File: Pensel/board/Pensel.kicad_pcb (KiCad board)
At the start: 2 copper layers, 60 x 13 mm, 189 parts, among them J1 TEST_1P, J2 Fiducial, J3 JTAG, J4 I2C, J5 Fiducial, J6 Fiducial, J7 Fiducial, J8 UART, P1 USB_PROC, SW1 RST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

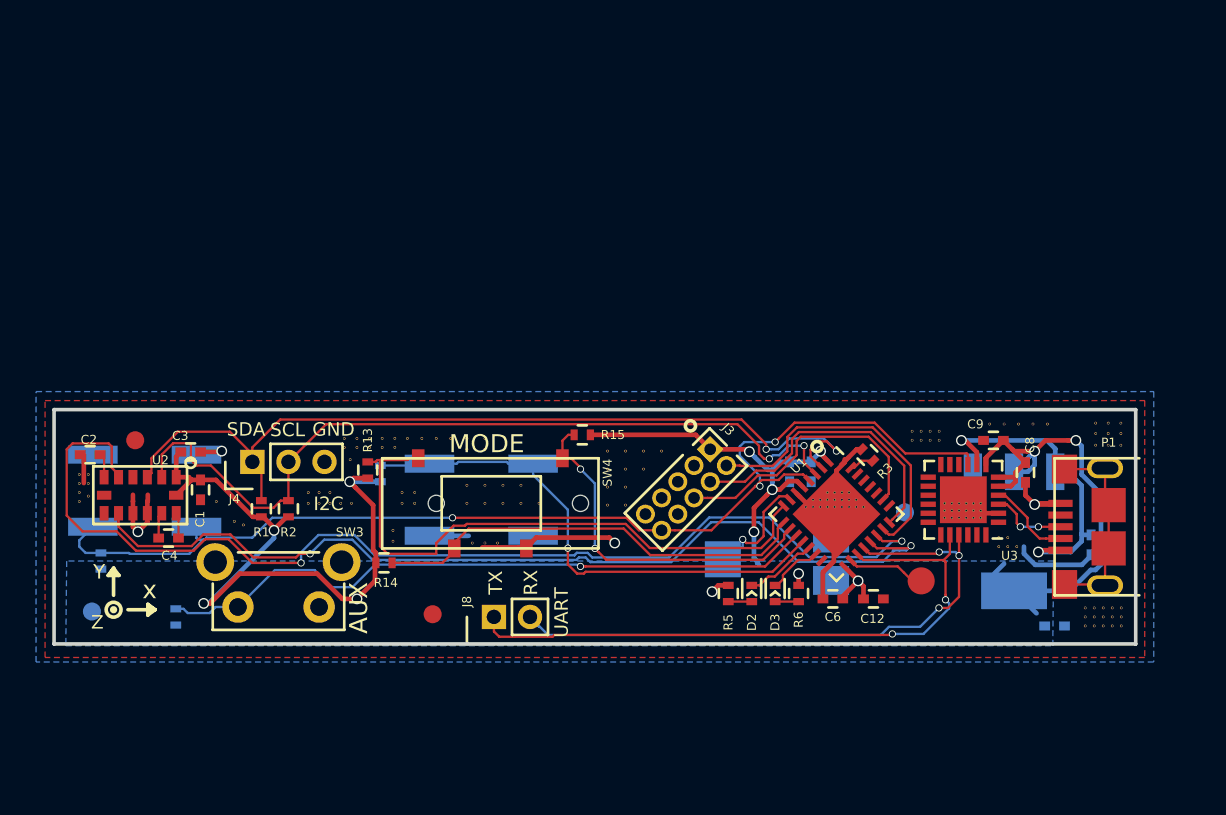
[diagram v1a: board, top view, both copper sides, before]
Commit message: Many changes supporting board revision 2.0
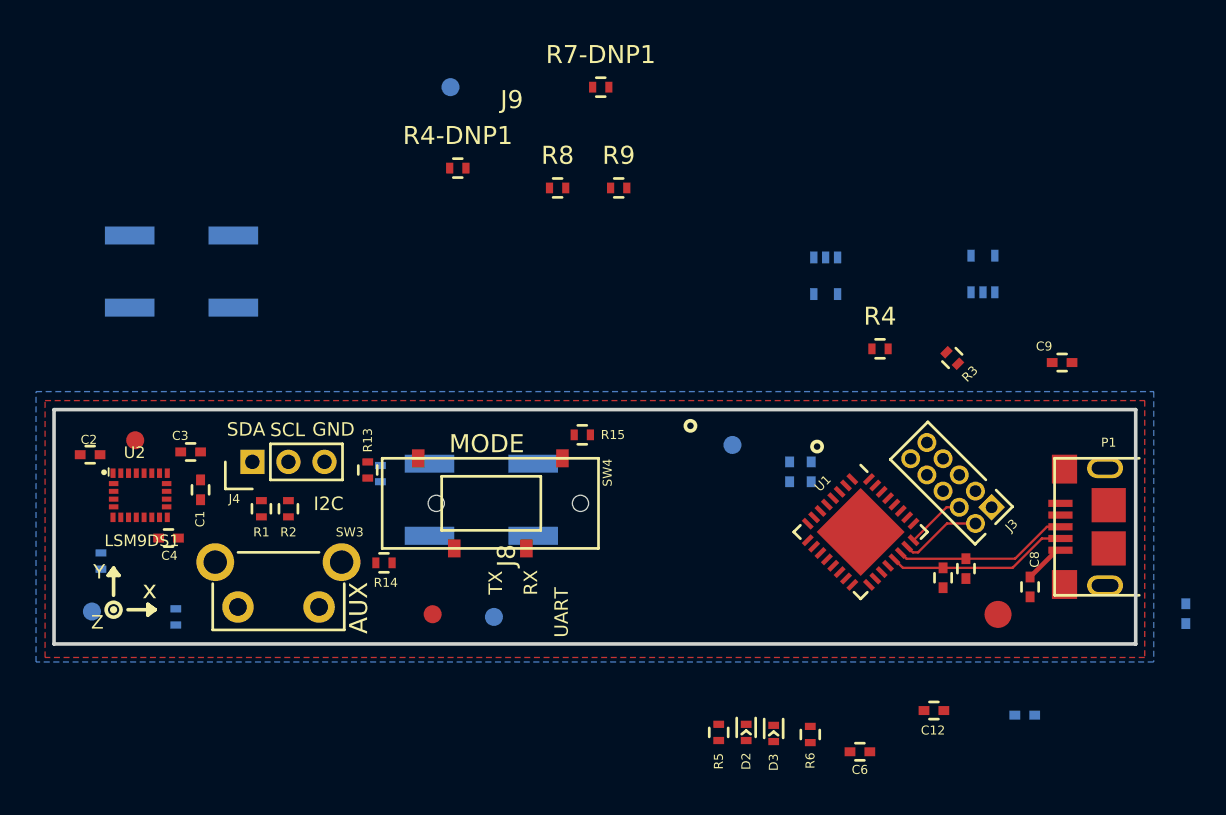
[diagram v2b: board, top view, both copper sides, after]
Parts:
- removed ? (x146): via-1.0mm, TylerCustom:via-1.0mm
- removed RV10K1: THUMBWHEEL, TylerCustom:ST-4
- added C_NOSTUFF1: 0.1 uF, Capacitors_SMD:C_0402, F.Cu at (100.6, 147.3)
- added C_NOSTUFF2: 0.1 uF, Capacitors_SMD:C_0402, F.Cu at (99.3, 147.8)
- added J9: UART_RX, Fiducials:Fiducial_1mm_Dia_2.54mm_Outer_CopperBottom, F.Cu at (72.0, 120.6)
- added R4: 4K7, Resistors_SMD:R_0402, F.Cu at (95.8, 135.1)
- added R4-DNP1: 4K7, Resistors_SMD:R_0402, F.Cu at (72.4, 125.1)
- added R7-DNP1: 4K7, Resistors_SMD:R_0402, F.Cu at (80.3, 120.6)
- added R8: 4K7, Resistors_SMD:R_0402, F.Cu at (77.9, 126.2)
- added R9: 4K7, Resistors_SMD:R_0402, F.Cu at (81.3, 126.2)
- C1: value 4.7 uF -> 10 nF
- C2: value 4.7 uF -> 0.1 uF
- C3: value 0.1 uF -> 10 nF
- C4: value 0.22 uF -> 0.1 uF
- C8: value 4.7 uF -> 1 uF
- C9: value 0.1 uF -> 1 uF
- J8: value UART -> UART_TX; footprint Pin_Headers:Pin_Header_Straight_1x02_Pitch2.00mm -> Fiducials:Fiducial_1mm_Dia_2.54mm_Outer_CopperBottom
- U2: value LSM303DLHC -> LSM9DS1; footprint TylerCustom:LGA_14L_3mm_5mm -> LSM9DS1:PQFN24P43_350X300X102L35X23N
- U3: value CP2102N-A01-GQFN24 -> NCP114; footprint Housings_DFN_QFN:QFN-24-1EP_4x4mm_Pitch0.5mm -> TO_SOT_Packages_SMD:SC-70-5; moved to B.Cu
- U4: value AP111733 -> NCP508; footprint TO_SOT_Packages_SMD:SOT-223 -> TO_SOT_Packages_SMD:SC-70-5
- moved U4 17.6 mm to (92.8, 131.1)
- moved J3 15.9 mm to (102.0, 143.9), turned to 225 degrees
- moved U3 12.6 mm to (101.5, 131.0)
- moved SW1 12.3 mm to (57.1, 130.8)
- moved J2 10.3 mm to (87.6, 140.5)
- moved C6 8.61 mm to (94.7, 157.5)
- moved R6 7.85 mm to (91.9, 156.5)
- moved D3 7.76 mm to (89.9, 156.5)
- moved R5 7.72 mm to (86.9, 156.4)
- moved D2 7.71 mm to (88.4, 156.4)
- moved R3 7.15 mm to (99.8, 135.6)
- moved C12 7.04 mm to (98.8, 155.2)
- moved C11 6.49 mm to (112.8, 149.8)
- moved C8 6.36 mm to (104.1, 148.3)
- moved C9 5.76 mm to (105.9, 135.9)
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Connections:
- net Net-(J1-Pad1) renamed /test_pin
- net Net-(R3-Pad1) renamed /boot
- C1 pad 1: +3V3 -> +3.3VA
- C2 pad 1: Net-(C2-Pad1) -> +3.3VA
- C3 pad 1: +3V3 -> Net-(C3-Pad1)
- C4 pad 2: Net-(C4-Pad2) -> GND
- C8 pad 1: +3V3 -> +5V
- C9 pad 1: +3V3 -> +3.3VA
- J3 pad 7: Net-(J3-Pad7) -> (no net)
- J3 pad 8: Net-(J3-Pad8) -> (no net)
- P1 pad 2: Net-(P1-Pad2) -> /USB_n
- P1 pad 3: Net-(P1-Pad3) -> /USB_p
- P1 pad 4: Net-(P1-Pad4) -> (no net)
- U1 pad 15: Net-(U1-Pad15) -> (no net)
- U1 pad 19: DBG_UART_TX -> (no net)
- U1 pad 20: DBG_UART_RX -> (no net)
- U1 pad 21: SEN_DRDY -> /USB_n
- U1 pad 22: SEN_INT1 -> /USB_p
- U1 pad 25: Net-(U1-Pad25) -> (no net)
- U1 pad 27: Net-(U1-Pad27) -> (no net)
- U1 pad 28: Net-(U1-Pad28) -> (no net)
- U1 pad 29: Net-(U1-Pad29) -> BREV-0
- U1 pad 30: Net-(U1-Pad30) -> BREV-1
- U1 pad 5: +3V3 -> +3.3VA
- U1 pad 7: THUMBWHEEL -> (no net)
- U2 pad 10: GND -> (no net)
- U2 pad 11: GND -> (no net)
- U2 pad 12: Net-(C4-Pad2) -> (no net)
- U2 pad 13: Net-(C4-Pad1) -> +3V3
- U2 pad 14: +3V3 -> GND
- U2 pad 3: SDA -> +3V3
- U2 pad 4: Net-(U2-Pad4) -> SDA
- U2 pad 5: SEN_INT1 -> +3V3
- U2 pad 6: Net-(C2-Pad1) -> +3V3
- U2 pad 7: GND -> +3V3
- U2 pad 8: Net-(U2-Pad8) -> +3V3
- U2 pad 9: SEN_DRDY -> (no net)
- U3 pad 1: Net-(U3-Pad1) -> +5V
- U3 pad 3: Net-(P1-Pad3) -> +5V
- U3 pad 4: Net-(P1-Pad2) -> (no net)
- U4 pad 1: GND -> +5V
- U4 pad 2: +3V3 -> GND
- U4 pad 3: +5V -> +3V3
- U4 pad 4: +3V3 -> (no net)
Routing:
- net +3V3: track 94.1 -> 0.00 mm, vias 13 -> 0
- net RESET_n: track 63.1 -> 0.00 mm, vias 3 -> 0
- net SEN_INT1: track 61.8 -> 0.00 mm, vias 2 -> 0
- net SEN_DRDY: track 52.1 -> 0.00 mm, vias 2 -> 0
- net SDA: track 49.1 -> 0.00 mm, vias 2 -> 0
- net SCL: track 45.5 -> 0.00 mm, vias 2 -> 0
- net GND: track 38.0 -> 0.00 mm, vias 4 -> 0
- net BTN_AUX: track 37.2 -> 0.00 mm, vias 1 -> 0
- net DBG_UART_TX: track 36.2 -> 0.00 mm, vias 2 -> 0
- net DBG_UART_RX: track 34.8 -> 0.00 mm, vias 3 -> 0
- net MODE_0: track 33.8 -> 0.00 mm
- net BTN_MAIN: track 29.0 -> 0.00 mm, vias 1 -> 0
- net MODE_1: track 24.5 -> 0.00 mm
- net MODE_2: track 19.7 -> 0.00 mm, vias 2 -> 0
- net SWD-SWO: track 15.6 -> 0.00 mm
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- removed copper zone on B.Cu, net +3V3

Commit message: first time fully routed and placed v2
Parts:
- removed J8: UART_TX, Fiducials:Fiducial_1mm_Dia_2.54mm_Outer_CopperBottom
- removed J9: UART_RX, Fiducials:Fiducial_1mm_Dia_2.54mm_Outer_CopperBottom
- removed R4-DNP1, R7-DNP1: 4K7, Resistors_SMD:R_0402
- added ?: via-1.0mm, TylerCustom:via-1.0mm, F.Cu at (94.5, 145.5)
- added ?: via-1.0mm, TylerCustom:via-1.0mm, F.Cu at (94.5, 144.0)
- added ?: via-1.0mm, TylerCustom:via-1.0mm, F.Cu at (95.2, 144.0)
- added ?: via-1.0mm, TylerCustom:via-1.0mm, F.Cu at (96.8, 144.0)
- added ?: via-1.0mm, TylerCustom:via-1.0mm, F.Cu at (96.0, 144.0)
- added ?: via-1.0mm, TylerCustom:via-1.0mm, F.Cu at (96.0, 143.2)
- added ?: via-1.0mm, TylerCustom:via-1.0mm, F.Cu at (95.2, 143.2)
- added ?: via-1.0mm, TylerCustom:via-1.0mm, F.Cu at (94.5, 143.2)
- added ?: via-1.0mm, TylerCustom:via-1.0mm, F.Cu at (95.2, 142.5)
- added ?: via-1.0mm, TylerCustom:via-1.0mm, F.Cu at (94.5, 142.5)
- added ?: via-1.0mm, TylerCustom:via-1.0mm, F.Cu at (95.2, 145.5)
- added ?: via-1.0mm, TylerCustom:via-1.0mm, F.Cu at (96.0, 144.8)
- added ?: via-1.0mm, TylerCustom:via-1.0mm, F.Cu at (95.2, 144.8)
- added ?: via-1.0mm, TylerCustom:via-1.0mm, F.Cu at (94.5, 144.8)
- added ?: via-1.0mm, TylerCustom:via-1.0mm, F.Cu at (93.8, 144.8)
- added ?: via-1.0mm, TylerCustom:via-1.0mm, F.Cu at (93.0, 144.0)
- added ?: via-1.0mm, TylerCustom:via-1.0mm, F.Cu at (93.8, 143.2)
- added ?: via-1.0mm, TylerCustom:via-1.0mm, F.Cu at (93.8, 144.0)
- added C13: 0.1 uF, Capacitors_SMD:C_0402, F.Cu at (91.5, 141.2)
- added C14: 1 uF, Capacitors_SMD:C_0402, F.Cu at (89.8, 142.8)
- added JP1: Jumper, Resistors_SMD:R_0402, F.Cu at (108.0, 139.9)
- C1: value 10 nF -> 10 uF; footprint Capacitors_SMD:C_0402 -> Capacitors_SMD:c_elec_3x5.3
- C10, C11, C5, R10, R11, R12, U3, U4: moved to F.Cu
- C7: value 1 uF -> 0.1 uF; moved to F.Cu
- J4: value I2C -> COMS; footprint Pin_Headers:Pin_Header_Straight_1x03_Pitch2.00mm -> Pin_Headers:Pin_Header_Straight_1x06_Pitch2.00mm
- SW1: value RST -> TACT_4.2MM; footprint Buttons_Switches_SMD:SW_SPST_B3SL-1002P -> MF_Switches:MF_Switches-TACT4.2MM; moved to F.Cu
- SW3: footprint Buttons_Switches_ThroughHole:SW_Tactile_SPST_Angled -> Buttons_Switches_SMD:SW_SPST_B3SL-1002P
- moved R10 47.2 mm to (99.6, 143.1), turned to 180 degrees
- moved C12 46.3 mm to (53.1, 147.6), turned to 270 degrees
- moved R3 26.3 mm to (74.4, 142.5), turned to 270 degrees
- moved J4 25.5 mm to (85.1, 149.6), turned to 270 degrees
- moved R8 22.8 mm to (96.2, 139.8), turned to 45 degrees
- moved R9 21.5 mm to (97.2, 140.8), turned to 45 degrees
- moved U4 21.1 mm to (103.5, 149.3), turned to 180 degrees
- moved R1 19.0 mm to (80.3, 147.1), turned to 270 degrees
- moved U3 18.2 mm to (98.3, 148.8)
- moved SW2 17.8 mm to (56.0, 145.1)
- moved J2 17.5 mm to (102.7, 149.4)
- moved C6 16.0 mm to (90.7, 142.0), turned to 135 degrees
- moved SW1 15.7 mm to (69.3, 140.7), turned to 0 degrees
- moved R2 15.3 mm to (78.0, 147.1), turned to 270 degrees
- moved J5 15.2 mm to (64.0, 140.3)
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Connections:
- net /USB_n renamed /USB-
- net /USB_p renamed /USB+
- C6 pad 1: +3V3 -> +3.3VA
- J4 pad 1: SDA -> +3V3
- J4 pad 2: SCL -> UART_TX
- J4 pad 3: GND -> UART_RX
- R3 pad 1: /boot -> Net-(R3-Pad1)
- R4 pad 1: +3V3 -> Net-(R4-Pad1)
- R4 pad 2: GND -> +3V3
- SW1 pad 1: GND -> +3V3
- SW1 pad 2: RESET_n -> (no net)
- U1 pad 15: (no net) -> M_DRDY
- U1 pad 19: (no net) -> UART_TX
- U1 pad 20: (no net) -> UART_RX
- U1 pad 25: (no net) -> AG_INT2
- U1 pad 31: /boot -> Net-(R3-Pad1)
- U1 pad 7: (no net) -> AG_INT1
- U2 pad 11: (no net) -> AG_INT1
- U2 pad 12: (no net) -> AG_INT2
- U2 pad 9: (no net) -> M_DRDY
- U4 pad 3: +3V3 -> Net-(R4-Pad1)
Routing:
- net +3V3: track 0.00 -> 89.7 mm, vias 0 -> 8
- net GND: track 0.00 -> 88.2 mm, vias 0 -> 15
- net SDA: track 0.00 -> 64.7 mm, vias 0 -> 2
- net SCL: track 0.00 -> 63.0 mm, vias 0 -> 4
- net AG_INT2: track 0.00 -> 48.2 mm, vias 0 -> 2
- net BTN_MAIN: track 0.00 -> 45.4 mm, vias 0 -> 2
- net AG_INT1: track 0.00 -> 41.9 mm, vias 0 -> 4
- net M_DRDY: track 0.00 -> 41.4 mm, vias 0 -> 2
- net Net-(R3-Pad1): track 0.00 -> 35.7 mm
- net BTN_AUX: track 0.00 -> 31.6 mm, vias 0 -> 2
- net +3.3VA: track 0.00 -> 24.7 mm, vias 0 -> 4
- net MODE_0: track 0.00 -> 23.0 mm, vias 0 -> 2
- net UART_RX: track 0.00 -> 21.4 mm, vias 0 -> 1
- net UART_TX: track 0.00 -> 18.3 mm, vias 0 -> 1
- net MODE_1: track 0.00 -> 14.3 mm, vias 0 -> 2
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- added copper zone on In2.Cu, net +3.3VA
- added copper zone on In2.Cu, net +3V3
- added copper zone on In1.Cu, net GND
- removed copper zone on B.Cu, net GND
- removed copper zone on F.Cu, net GND
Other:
- copper layers 2 -> 4
- board text added: "2.0 3/18 Tyler Holmes"
- board text added: "DFU"
- board text removed: "1.0 3/17 Tyler Holmes"
- board text removed: "3V3"
- board text removed: "5V0"
- board text removed: "I2C"
- board text removed: "RST"
- board text removed: "SENSITIVITY"
- board text removed: "UART"

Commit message: finalized footprints and layout for v2 hopefully
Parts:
- C1: footprint Capacitors_SMD:c_elec_3x5.3 -> Capacitors_SMD:C_0603
- moved C1 2.12 mm to (56.9, 142.8), turned to 90 degrees
- moved SW2 0.56 mm to (55.5, 144.9)
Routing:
- net +3.3VA: track 24.7 -> 17.2 mm, vias 4 -> 3
- net GND: track 88.2 -> 87.1 mm
- net SDA: track 64.7 -> 63.6 mm
- net SCL: track 63.0 -> 62.0 mm

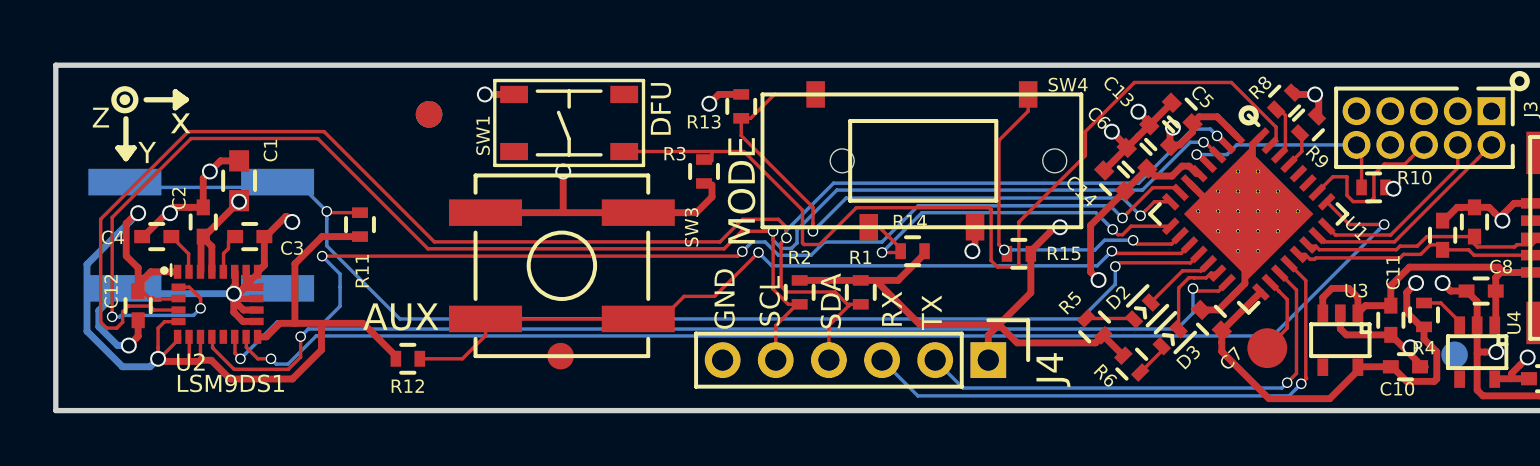
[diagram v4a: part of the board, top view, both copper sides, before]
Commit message: reorganize pins, add oscillator to support USB
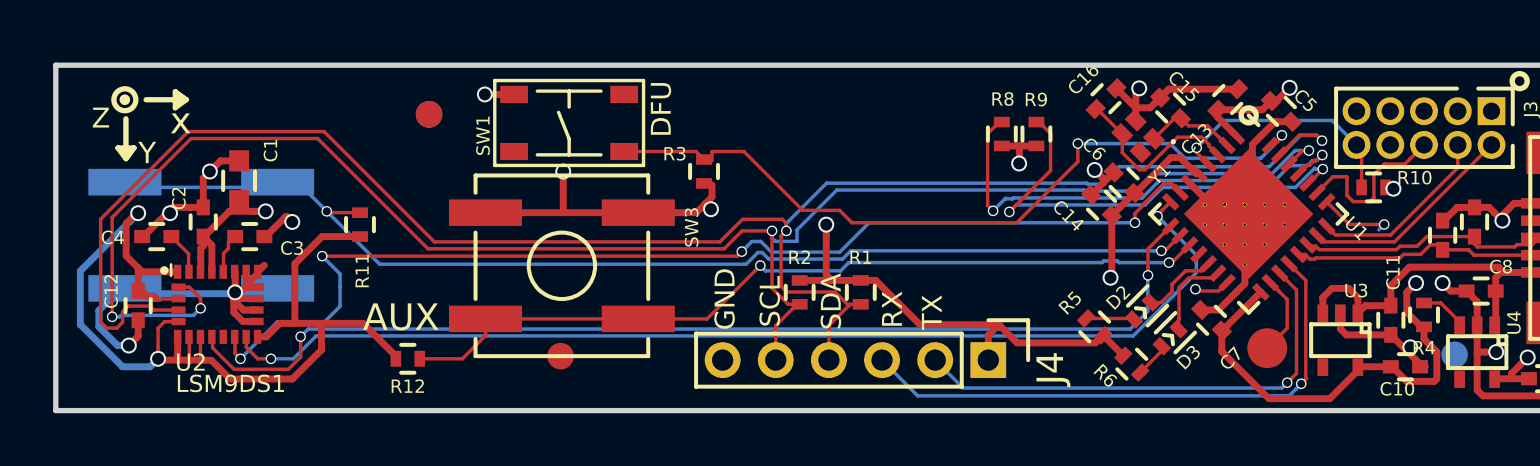
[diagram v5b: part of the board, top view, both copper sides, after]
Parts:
- removed the ? at (94.5, 145.5)
- removed the ? at (94.5, 144.0)
- removed the ? at (95.2, 144.0)
- removed the ? at (96.8, 144.0)
- removed the ? at (96.0, 144.0)
- removed the ? at (96.0, 143.2)
- removed the ? at (95.2, 143.2)
- removed the ? at (94.5, 143.2)
- removed the ? at (95.2, 142.5)
- removed the ? at (94.5, 142.5)
- removed the ? at (95.2, 145.5)
- removed the ? at (96.0, 144.8)
- removed the ? at (95.2, 144.8)
- removed the ? at (94.5, 144.8)
- removed the ? at (93.8, 144.8)
- removed the ? at (93.0, 144.0)
- removed the ? at (93.8, 143.2)
- removed the ? at (93.8, 144.0)
- removed R13, R14, R15: 4K7, Resistors_SMD:R_0402
- removed SW4: MODE_SEL, TylerCustom:CL-SB-13B-01
- added ?: via-1.0mm, TylerCustom:via-1.0mm, F.Cu at (94.0, 145.2)
- added ?: via-1.0mm, TylerCustom:via-1.0mm, F.Cu at (96.2, 143.8)
- added ?: via-1.0mm, TylerCustom:via-1.0mm, F.Cu at (96.2, 144.5)
- added ?: via-1.0mm, TylerCustom:via-1.0mm, F.Cu at (95.5, 144.5)
- added ?: via-1.0mm, TylerCustom:via-1.0mm, F.Cu at (95.5, 145.2)
- added ?: via-1.0mm, TylerCustom:via-1.0mm, F.Cu at (94.8, 145.2)
- added ?: via-1.0mm, TylerCustom:via-1.0mm, F.Cu at (94.8, 146.0)
- added ?: via-1.0mm, TylerCustom:via-1.0mm, F.Cu at (94.8, 144.5)
- added ?: via-1.0mm, TylerCustom:via-1.0mm, F.Cu at (94.0, 144.5)
- added ?: via-1.0mm, TylerCustom:via-1.0mm, F.Cu at (93.2, 144.5)
- added ?: via-1.0mm, TylerCustom:via-1.0mm, F.Cu at (93.2, 143.8)
- added ? (x2): via-1.0mm, TylerCustom:via-1.0mm, F.Cu at (94.0, 143.8)
- added ?: via-1.0mm, TylerCustom:via-1.0mm, F.Cu at (94.8, 143.8)
- added ?: via-1.0mm, TylerCustom:via-1.0mm, F.Cu at (95.5, 143.8)
- added C15: 8 pF, Capacitors_SMD:C_0402, F.Cu at (92.0, 140.1)
- added C16: 8 pF, Capacitors_SMD:C_0402, F.Cu at (89.5, 139.8)
- added Y1: 24 MHz, 416F32022CKR:OSCSC49P160X120X45-4N, F.Cu at (90.7, 141.2)
- moved R8 10.7 mm to (85.6, 141.1), turned to 270 degrees
- moved R9 10.2 mm to (86.9, 141.1), turned to 270 degrees
- moved C5 3.73 mm to (96.1, 140.2), turned to 315 degrees
- moved C13 2.90 mm to (94.1, 139.8), turned to 45 degrees
- moved C14 1.04 mm to (89.4, 143.8)
- moved C6 1.04 mm to (90.2, 142.9)
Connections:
- J3 pad 7: (no net) -> Net-(J3-Pad7)
- J3 pad 8: (no net) -> Net-(J3-Pad8)
- P1 pad 4: (no net) -> Net-(P1-Pad4)
- SW1 pad 2: (no net) -> Net-(SW1-Pad2)
- SW1 pad 3: (no net) -> Net-(SW1-Pad3)
- U1 pad 10: MODE_2 -> BTN_MAIN
- U1 pad 12: BTN_MAIN -> Net-(U1-Pad12)
- U1 pad 15: M_DRDY -> Net-(U1-Pad15)
- U1 pad 2: SDA -> Net-(C15-Pad1)
- U1 pad 25: AG_INT2 -> Net-(U1-Pad25)
- U1 pad 27: (no net) -> BREV-0
- U1 pad 28: (no net) -> BREV-1
- U1 pad 29: BREV-0 -> SCL
- U1 pad 3: SCL -> Net-(C16-Pad1)
- U1 pad 30: BREV-1 -> SDA
- U1 pad 8: MODE_0 -> AG_INT2
- U1 pad 9: MODE_1 -> M_DRDY
- U2 pad 10: (no net) -> Net-(U2-Pad10)
- U3 pad 4: (no net) -> Net-(U3-Pad4)
- U4 pad 4: (no net) -> Net-(U4-Pad4)
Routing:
- net MODE_0: track 23.0 -> 0.00 mm, vias 2 -> 0
- net BREV-1: track 1.98 -> 18.2 mm, vias 0 -> 2
- net BREV-0: track 1.42 -> 17.6 mm, vias 0 -> 2
- net MODE_1: track 14.3 -> 0.00 mm, vias 2 -> 0
- net MODE_2: track 13.3 -> 0.00 mm, vias 2 -> 0
- net AG_INT2: track 48.2 -> 41.2 mm
- net Net-(C16-Pad1): track 0.00 -> 6.77 mm
- net Net-(R3-Pad1): track 35.7 -> 29.2 mm, vias 0 -> 2
- net +3V3: track 89.7 -> 83.7 mm, vias 8 -> 7
- net SDA: track 63.6 -> 68.9 mm
- net SCL: track 62.0 -> 65.8 mm
- net Net-(C15-Pad1): track 0.00 -> 3.49 mm
- net BTN_MAIN: track 45.4 -> 42.3 mm
- net Net-(U1-Pad25): track 0.00 -> 2.87 mm, vias 0 -> 1
- net GND: track 87.1 -> 89.1 mm
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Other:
- board text removed: "MODE"

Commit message: minor cleanup & add some silk
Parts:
- removed the ? at (96.2, 143.8)
- added ?: via-1.0mm, TylerCustom:via-1.0mm, F.Cu at (94.0, 143.0)
- added ?: via-1.0mm, TylerCustom:via-1.0mm, F.Cu at (94.8, 143.0)
- moved J7 18.0 mm to (86.7, 146.2)
- moved SW1 11.7 mm to (81.0, 141.0)
- moved C16 1.66 mm to (89.7, 141.4), turned to 135 degrees
- moved J5 1.57 mm to (62.5, 140.3)
- moved J6 1.57 mm to (62.5, 140.3)
- moved C15 1.43 mm to (90.6, 139.8), turned to 225 degrees
- moved SW3 1.27 mm to (69.0, 144.8)
- moved Y1 1.09 mm to (91.8, 140.9), turned to 225 degrees
- moved C14 0.88 mm to (88.9, 143.0), turned to 225 degrees
- moved C6 0.37 mm to (90.6, 143.1), turned to 225 degrees
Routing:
- net Net-(R3-Pad1): track 29.2 -> 36.7 mm
- net +3V3: track 83.7 -> 87.6 mm
- net Net-(U1-Pad25): track 2.87 -> 0.07 mm, vias 1 -> 0
- net +3.3VA: track 17.4 -> 19.8 mm
- net Net-(C16-Pad1): track 6.77 -> 4.41 mm
- net Net-(JP1-Pad2): track 13.1 -> 15.5 mm
- net BREV-0: track 17.6 -> 18.7 mm
- net AG_INT2: track 41.2 -> 40.1 mm
- net GND: track 89.1 -> 90.1 mm
- net M_DRDY: track 40.9 -> 40.1 mm
- net Net-(C15-Pad1): track 3.49 -> 4.26 mm
- net SWD-SWO: track 6.46 -> 5.71 mm
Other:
- board text added: "3v3"
- board text added: "analog"
- board text added: "digital"
